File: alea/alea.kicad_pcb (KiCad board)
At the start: 4 copper layers, 111 x 99.9 mm, 47 parts, among them J1 QL_SLOT_DIN41612, J2 Conn_02x17_Odd_Even, J3 Conn_01x03_Pin, Q1 BC109, U0 LM340T-5, U1 68000D, U10 MSM514400D, U11 MSM514400D, U12 DP4873V, U2 EP1810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

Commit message: remove last extra vias
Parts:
- moved BT1 41.8 mm to (163.7, 51.4), turned to 0 degrees
- moved D2 8.64 mm to (169.9, 65.3), turned to 0 degrees
- moved D1 8.64 mm to (169.9, 61.7), turned to 0 degrees
- moved C8 8.24 mm to (157.4, 46.6), turned to -90 degrees
- moved C9 7.47 mm to (151.4, 53.7), turned to 0 degrees
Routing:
- net Net-(BT1--): track 54.2 -> 15.4 mm
- net /IPL1: track 140.0 -> 133.3 mm
- net GND: track 813.1 -> 807.3 mm
- net /IPL0: track 129.7 -> 126.0 mm
- net +9V: track 108.7 -> 112.0 mm
- net +5V: track 534.1 -> 535.7 mm
- net /DG8: track 129.6 -> 128.4 mm
- net /RDW: track 127.2 -> 126.6 mm
- net /FDC_IP: track 28.7 -> 29.3 mm
- net /RESFDC: track 85.0 -> 85.6 mm
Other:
- board text added: "Backplane 5V"
- board text added: "QL 9V"
- board text removed: "Backplane (5V)"
- board text removed: "QL (9V)"

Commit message: remove last extra vias
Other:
- board text added: "DP4873V"
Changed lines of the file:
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@@
 		(tags "Resistor Axial_DIN0204 series Axial Horizontal pin pitch 7.62mm 0.167W length 3.6mm diameter 1.6mm")
 		(property "Reference" "R3"
-			(at 3.81 0 0)
+			(at 9.906 0 0)
 			(layer "F.SilkS")
 			(effects
@@
 		(tags "Diode DO-35_SOD27 series Axial Horizontal pin pitch 7.62mm  length 4mm diameter 2mm")
 		(property "Reference" "D1"
-			(at 4.064 0 0)
+			(at -2.2352 0 0)
 			(layer "F.SilkS")
 			(effects
@@
 		(tags "C Disc series Radial pin pitch 2.50mm  diameter 3.0mm width 1.6mm Capacitor")
 		(property "Reference" "C1"
-			(at -1.9758 -0.0254 0)
+			(at 4.552 -0.0254 0)
 			(layer "F.SilkS")
 			(effects
@@
 		(tags "plcc leaded")
 		(property "Reference" "U2"
-			(at 0 -2.032 0)
+			(at -16.891 -1.905 0)
 			(layer "F.SilkS")
 			(effects
@@
 		(tags "plcc leaded")
 		(property "Reference" "U1"
-			(at -2.0828 -3.8608 0)
+			(at -16.764 -1.925 0)
 			(layer "F.SilkS")
 			(effects
@@
 		(tags "Resistor Axial_DIN0204 series Axial Horizontal pin pitch 7.62mm 0.167W length 3.6mm diameter 1.6mm")
 		(property "Reference" "R4"
-			(at 3.81 0 0)
+			(at 9.906 0 0)
 			(layer "F.SilkS")
 			(effects
@@
 		(tags "C Disc series Radial pin pitch 2.50mm  diameter 3.0mm width 1.6mm Capacitor")
 		(property "Reference" "C2"
-			(at -1.9558 0.0254 0)
+			(at 4.572 0.0254 0)
 			(layer "F.SilkS")
 			(effects
@@
 		(tags "Diode DO-35_SOD27 series Axial Horizontal pin pitch 7.62mm  length 4mm diameter 2mm")
 		(property "Reference" "D3"
-			(at 3.81 0 90)
+			(at 3.556 1.905 90)
 			(layer "F.SilkS")
 			(effects
@@
 		(tags "plcc leaded")
 		(property "Reference" "U12"
-			(at -11.557 24.13 180)
+			(at -13.716 -1.524 270)
 			(layer "F.SilkS")
 			(effects
@@
 		(tags "Diode DO-35_SOD27 series Axial Horizontal pin pitch 7.62mm  length 4mm diameter 2mm")
 		(property "Reference" "D2"
-			(at 4.0132 0 0)
+			(at -2.286 0 0)
 			(layer "F.SilkS")
 			(effects
@@
 	)
 	(gr_circle
-		(center 145.4912 57.531)
-		(end 145.6944 57.8866)
+		(center 145.4658 57.277)
+		(end 145.669 57.6326)
 		(stroke
 			(width 0.15)
@@
 	)
 	(gr_circle
-		(center 148.3868 59.0042)
-		(end 148.59 59.3598)
+		(center 148.3614 58.7502)
+		(end 148.5646 59.1058)
 		(stroke
 			(width 0.15)
@@
 	)
 	(gr_circle
-		(center 146.9644 59.0042)
-		(end 147.1676 59.3598)
+		(center 146.939 58.7502)
+		(end 147.1422 59.1058)
 		(stroke
 			(width 0.15)
@@
 	)
 	(gr_circle
-		(center 148.3868 57.531)
-		(end 148.59 57.8866)
+		(center 148.3614 57.277)
+		(end 148.5646 57.6326)
 		(stroke
 			(width 0.15)
@@
 	)
 	(gr_line
-		(start 146.9136 59.0042)
-		(end 148.3868 59.0042)
+		(start 146.8882 58.7502)
+		(end 148.3614 58.7502)
 		(stroke
 			(width 0.889)
@@
 	)
 	(gr_circle
-		(center 146.9644 57.531)
-		(end 147.1676 57.8866)
+		(center 146.939 57.277)
+		(end 147.1422 57.6326)
 		(stroke
 			(width 0.15)
@@
 	)
 	(gr_line
-		(start 146.9136 57.531)
-		(end 148.3868 57.531)
+		(start 146.8882 57.277)
+		(end 148.3614 57.277)
 		(stroke
 			(width 0.889)
@@
 	)
 	(gr_circle
-		(center 145.4912 59.0042)
-		(end 145.6944 59.3598)
+		(center 145.4658 58.7502)
+		(end 145.669 59.1058)
 		(stroke
 			(width 0.15)
@@
 		)
 	)
+	(gr_text "DP4873V"
+		(at 157.861 122.682 0)
+		(layer "F.SilkS")
+		(effects
+			(font
+				(size 1 1)
+				(thickness 0.15)
+			)
+			(justify left bottom)
+		)
+	)
 	(gr_text "Backplane \n5V"
-		(at 145.6944 60.198 270)
+		(at 145.669 59.944 270)
 		(layer "F.SilkS")
 		(effects

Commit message: 2025/06 update
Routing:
- net GND: track 807.3 -> 815.5 mm
- net /A7: track 193.5 -> 200.2 mm
- net /AG9: track 95.4 -> 92.4 mm, vias 4 -> 3
- net /RESFDC: track 85.6 -> 88.4 mm
- net /DG15: track 79.1 -> 76.6 mm
- net /IPL0: track 126.0 -> 128.4 mm
- net /A2: track 126.5 -> 124.3 mm
- net /DG13: track 90.2 -> 88.1 mm
- net /DG14: track 96.6 -> 94.5 mm
- net /RW: track 189.6 -> 191.5 mm, vias 4 -> 5
- net /AG11: track 92.9 -> 91.1 mm, vias 3 -> 2
- net Net-(Q1-C): track 105.2 -> 107.0 mm
- net /AG17: track 57.1 -> 55.3 mm, vias 2 -> 0
- net /DG11: track 110.9 -> 109.3 mm
- net +5V: track 535.7 -> 537.3 mm
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
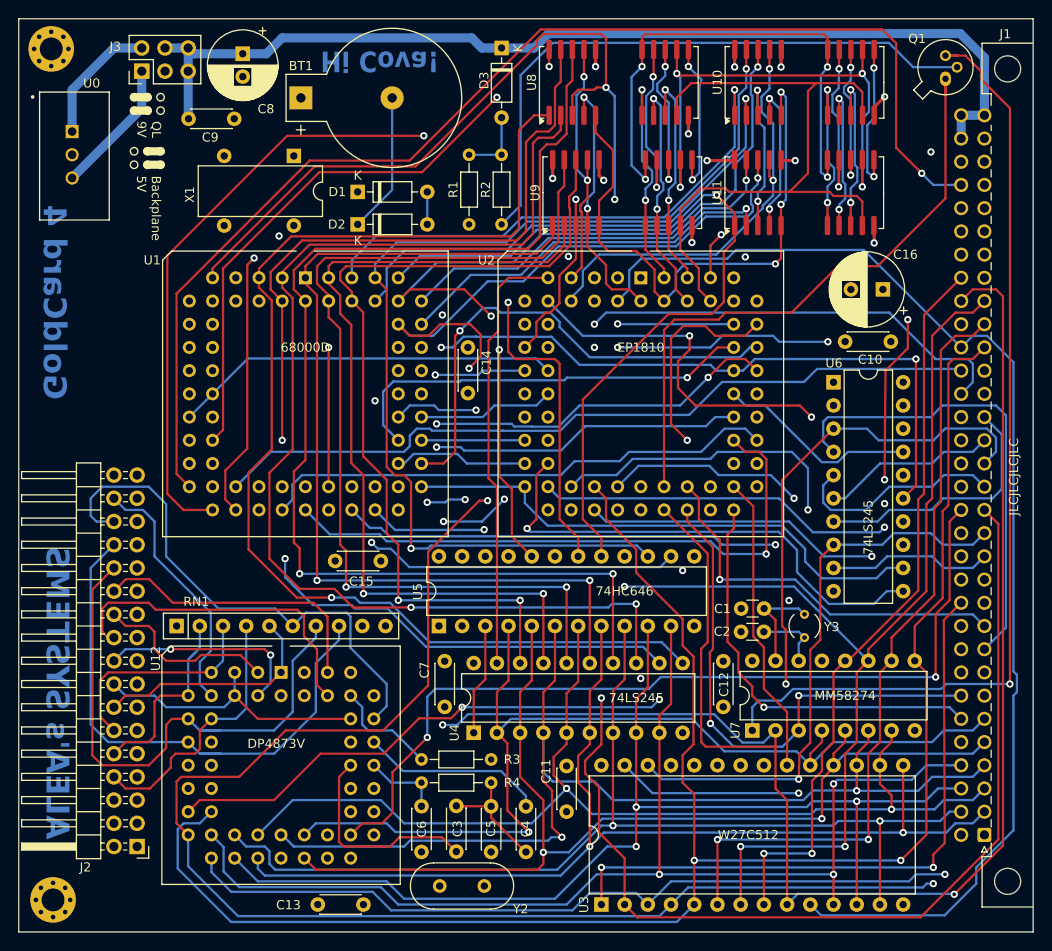
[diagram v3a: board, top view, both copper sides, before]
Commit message: update again for bad FDC pinout
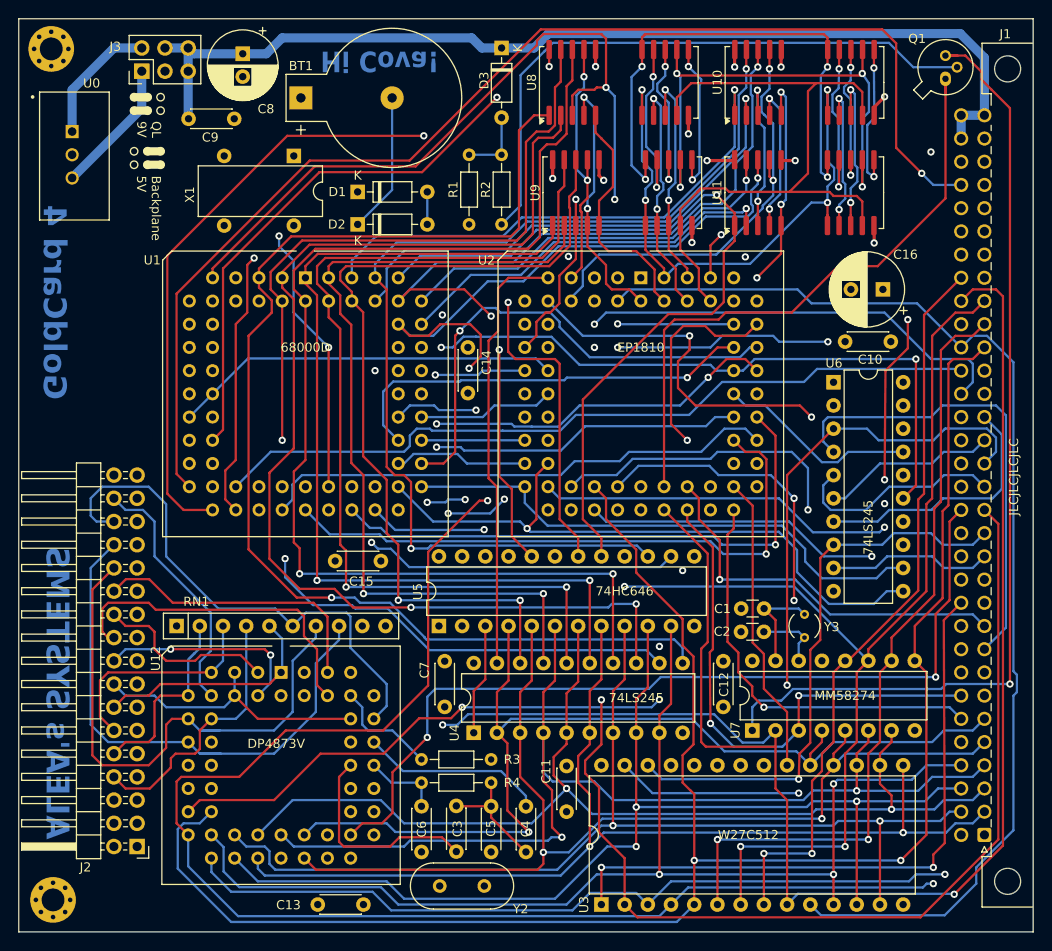
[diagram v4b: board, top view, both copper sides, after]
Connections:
- U12 pad 2: (no net) -> GND
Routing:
- net GND: track 815.5 -> 823.2 mm
- net /A0: track 132.1 -> 127.3 mm
- net /RESFDC: track 88.4 -> 84.9 mm
- net /MA7: track 81.2 -> 83.8 mm
- net /A7: track 200.2 -> 198.6 mm
- net /AG14: track 72.0 -> 70.6 mm
- net /MA9: track 64.0 -> 62.8 mm
- net /DG0: track 130.0 -> 131.0 mm
- net /A2: track 124.3 -> 123.5 mm
- net /DG11: track 109.3 -> 108.7 mm
- net /AG8: track 78.3 -> 77.8 mm

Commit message: fix values
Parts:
- added C17: 100n, Capacitor_THT:C_Disc_D4.3mm_W1.9mm_P5.00mm, F.Cu at (224.5, 109.9)
- C1, C2: value C -> 22p
- Q1: value BC109 -> BC548
- R1, R2: value R -> 1K
- Y3: value Crystal -> 32768hz
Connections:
- U6 pad 18: unconnected-(U6-B0-Pad18) -> GND
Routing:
- net /CAS1: track 47.0 -> 63.8 mm
- net +5V: track 537.3 -> 553.4 mm
- net /A4: track 131.2 -> 134.2 mm
- net /A3: track 124.1 -> 126.3 mm
- net /DTACK: track 76.0 -> 78.1 mm
- net Net-(D1-A): track 101.5 -> 103.4 mm
- net /A11: track 79.7 -> 81.0 mm
- net GND: track 823.2 -> 824.1 mm, vias 8 -> 9
- net /FDC_RD: track 57.5 -> 56.6 mm
- net /MA4: track 67.1 -> 66.3 mm
- net /MA3: track 73.1 -> 73.9 mm
- net /DG14: track 94.5 -> 93.7 mm
- net /MA6: track 73.2 -> 74.1 mm
- net /AG1: track 47.2 -> 48.0 mm
- net /AG6: track 49.7 -> 50.3 mm
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
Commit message: small update in alea
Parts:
- moved H1 3.91 mm to (140.5, 139.2)
- moved H2 3.91 mm to (140.3, 46.1)
- moved U0 3.80 mm to (142.3, 56.3)
- moved BT1 1.56 mm to (165.3, 51.4)
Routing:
- net GND: track 824.1 -> 890.1 mm, vias 9 -> 10
- net +5V: track 553.4 -> 563.6 mm, vias 4 -> 5
- net Net-(Q1-B): track 67.5 -> 64.4 mm
- net /A0: track 127.3 -> 129.3 mm
- net Net-(J3-Pin_2): track 14.1 -> 12.2 mm
- net Net-(Q1-C): track 106.7 -> 105.2 mm
- net /VSYNC: track 96.0 -> 94.8 mm
- net /VPA: track 145.0 -> 146.0 mm
- net Net-(BT1--): track 15.4 -> 16.1 mm
- net /A6: track 221.6 -> 222.2 mm
- net /FDC_WPRT: track 61.3 -> 60.7 mm
- net /MA5: track 94.7 -> 94.1 mm
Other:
- board size 111 x 99.9 mm -> 107.1 x 99.9 mm
- board text added: "ALEA SYSTEMS"
- board text removed: "ALEA's SYSTEMS"
